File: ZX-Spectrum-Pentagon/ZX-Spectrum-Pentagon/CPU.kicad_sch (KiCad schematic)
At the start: 17 parts, among them U24 74HC245, U25 74HC245, U26 74HC245, U27 Z80CPU, U28 74HC244, U29 GAL16V8, U3 74HC14, U30 29F040, U31 74HC32

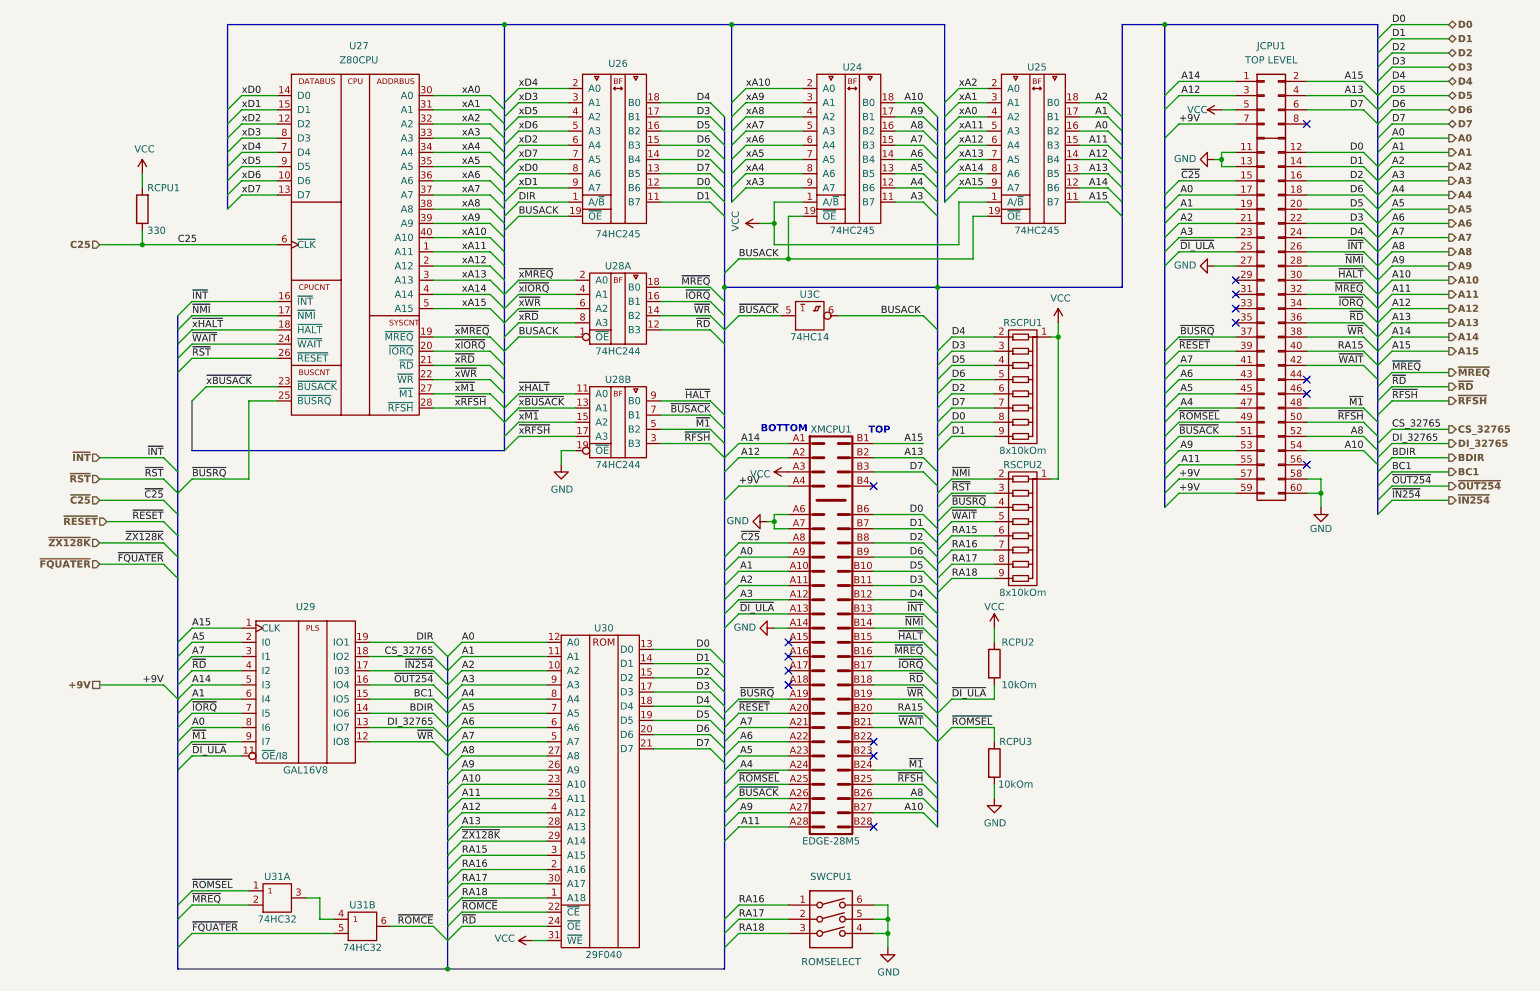
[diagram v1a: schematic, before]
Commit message: FDControlers rename from VCC1 to VDD zx_custom_symbol add connector Conn_02x32_Odd_Even ZX-Spectrum-Pentagon rename from +9V to POWER ZX-Spectrum-Perefiral improve schematic
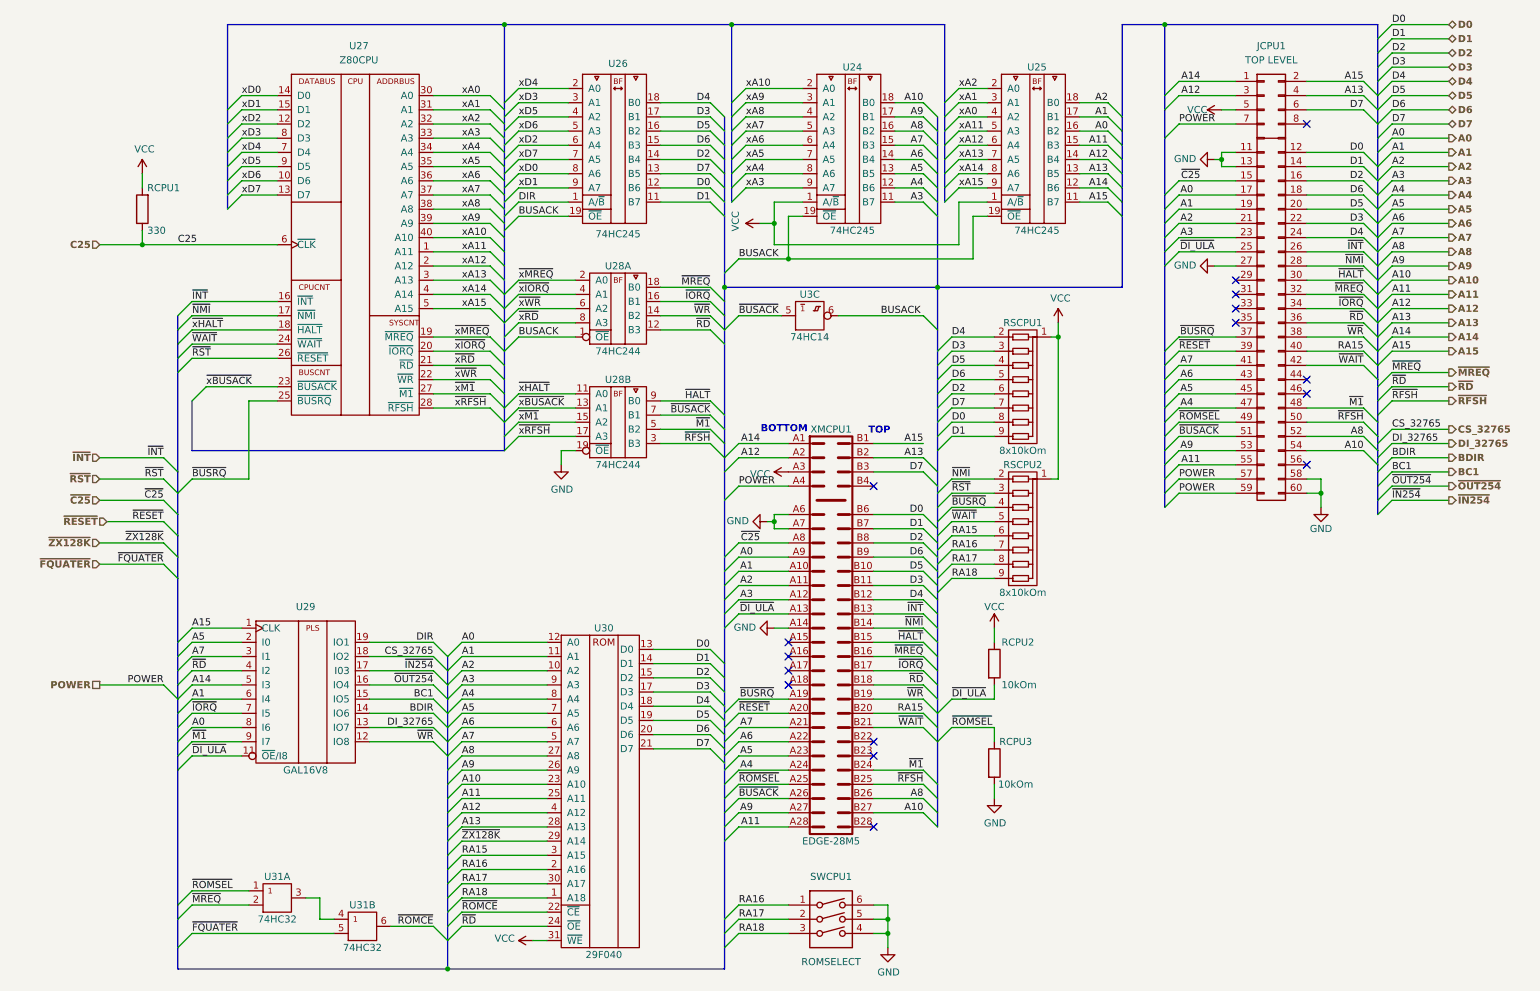
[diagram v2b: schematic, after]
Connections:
- net +9V renamed POWER
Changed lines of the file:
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@@
 		)
 	)
-	(label "+9V"
+	(label "POWER"
 		(at 35.56 133.35 180)
 		(fields_autoplaced yes)
@@
 		)
 	)
-	(label "+9V"
+	(label "POWER"
 		(at 217.17 33.02 0)
 		(fields_autoplaced yes)
@@
 		)
 	)
-	(label "+9V"
+	(label "POWER"
 		(at 217.17 99.06 0)
 		(fields_autoplaced yes)
@@
 		)
 	)
-	(label "+9V"
+	(label "POWER"
 		(at 217.17 96.52 0)
 		(fields_autoplaced yes)
@@
 		)
 	)
-	(label "+9V"
+	(label "POWER"
 		(at 138.43 97.79 0)
 		(fields_autoplaced yes)
@@
 		)
 	)
-	(hierarchical_label "+9V"
+	(hierarchical_label "POWER"
 		(shape passive)
 		(at 24.13 133.35 180)

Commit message: update pcb
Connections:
- net ~{ROMSEL} renamed ~{ROMEN}
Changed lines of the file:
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@@
 		)
 	)
-	(label "~{ROMSEL}"
+	(label "~{ROMEN}"
 		(at 217.17 86.36 0)
 		(fields_autoplaced yes)
@@
 		)
 	)
-	(label "~{ROMSEL}"
+	(label "~{ROMEN}"
 		(at 138.43 151.13 0)
 		(fields_autoplaced yes)
@@
 		)
 	)
-	(label "~{ROMSEL}"
+	(label "~{ROMEN}"
 		(at 176.53 140.97 0)
 		(fields_autoplaced yes)
@@
 		)
 	)
-	(label "~{ROMSEL}"
+	(label "~{ROMEN}"
 		(at 40.64 170.18 0)
 		(fields_autoplaced yes)
